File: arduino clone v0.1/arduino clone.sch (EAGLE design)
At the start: 24 parts, among them J202 FTDI Breakout Header, U101 ATMEGA328P_TQFP, U201 CH340G

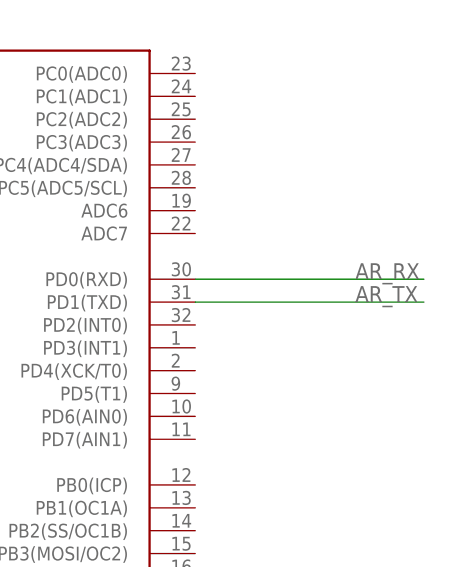
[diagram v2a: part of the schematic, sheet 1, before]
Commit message: connect MCU uart data lines to AR uart datalines
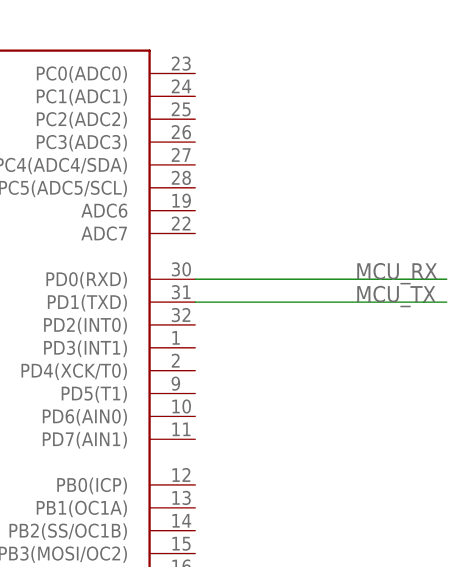
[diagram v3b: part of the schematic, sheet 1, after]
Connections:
- removed net AR_RX: R205.1, U101.PD0(RXD)
- removed net AR_TX: R206.1, U101.PD1(TXD)
- net MCU_RX: now also R205.1, U101.PD0(RXD)
- net MCU_TX: now also R206.1, U101.PD1(TXD)
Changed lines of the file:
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@@
 </segment>
 </net>
-<net name="AR_RX" class="0">
+<net name="MCU_RX" class="0">
 <segment>
 <pinref part="U101" gate="U$1" pin="PD0(RXD)"/>
 <wire x1="215.9" y1="139.7" x2="241.3" y2="139.7" width="0.1524" layer="91"/>
 <label x="233.68" y="139.7" size="1.778" layer="95"/>
-</segment>
-</net>
-<net name="AR_TX" class="0">
+<wire x1="241.3" y1="139.7" x2="243.84" y2="139.7" width="0.1524" layer="91"/>
+</segment>
+</net>
+<net name="MCU_TX" class="0">
 <segment>
 <pinref part="U101" gate="U$1" pin="PD1(TXD)"/>
 <wire x1="215.9" y1="137.16" x2="241.3" y2="137.16" width="0.1524" layer="91"/>
 <label x="233.68" y="137.16" size="1.778" layer="95"/>
+<wire x1="241.3" y1="137.16" x2="243.84" y2="137.16" width="0.1524" layer="91"/>
 </segment>
 </net>
@@
 </segment>
 </net>
-<net name="AR_RX" class="0">
-<segment>
-<pinref part="R205" gate="G$1" pin="1"/>
-<wire x1="312.42" y1="132.08" x2="320.04" y2="132.08" width="0.1524" layer="91"/>
-<wire x1="320.04" y1="132.08" x2="320.04" y2="129.54" width="0.1524" layer="91"/>
-<wire x1="320.04" y1="129.54" x2="350.52" y2="129.54" width="0.1524" layer="91"/>
-<label x="342.9" y="129.54" size="1.778" layer="95"/>
-</segment>
-</net>
-<net name="AR_TX" class="0">
-<segment>
-<pinref part="R206" gate="G$1" pin="1"/>
-<wire x1="312.42" y1="121.92" x2="320.04" y2="121.92" width="0.1524" layer="91"/>
-<wire x1="320.04" y1="121.92" x2="320.04" y2="124.46" width="0.1524" layer="91"/>
-<wire x1="320.04" y1="124.46" x2="350.52" y2="124.46" width="0.1524" layer="91"/>
-<label x="342.9" y="124.46" size="1.778" layer="95"/>
-</segment>
-</net>
 <net name="CH340G_DTR" class="0">
 <segment>
@@
 <label x="279.4" y="53.34" size="1.778" layer="95"/>
 </segment>
+<segment>
+<pinref part="R205" gate="G$1" pin="1"/>
+<wire x1="312.42" y1="132.08" x2="320.04" y2="132.08" width="0.1524" layer="91"/>
+<wire x1="320.04" y1="132.08" x2="320.04" y2="129.54" width="0.1524" layer="91"/>
+<wire x1="320.04" y1="129.54" x2="350.52" y2="129.54" width="0.1524" layer="91"/>
+<label x="342.9" y="129.54" size="1.778" layer="95"/>
+</segment>
 </net>
 <net name="FDTI_TX" class="0">
@@
 <label x="279.4" y="43.18" size="1.778" layer="95"/>
 </segment>
-</net>
+<segment>
+<pinref part="R206" gate="G$1" pin="1"/>
+<wire x1="312.42" y1="121.92" x2="320.04" y2="121.92" width="0.1524" layer="91"/>
+<wire x1="320.04" y1="121.92" x2="320.04" y2="124.46" width="0.1524" layer="91"/>
+<wire x1="320.04" y1="124.46" x2="350.52" y2="124.46" width="0.1524" layer="91"/>
+<label x="342.9" y="124.46" size="1.778" layer="95"/>
+</segment>
+</net>

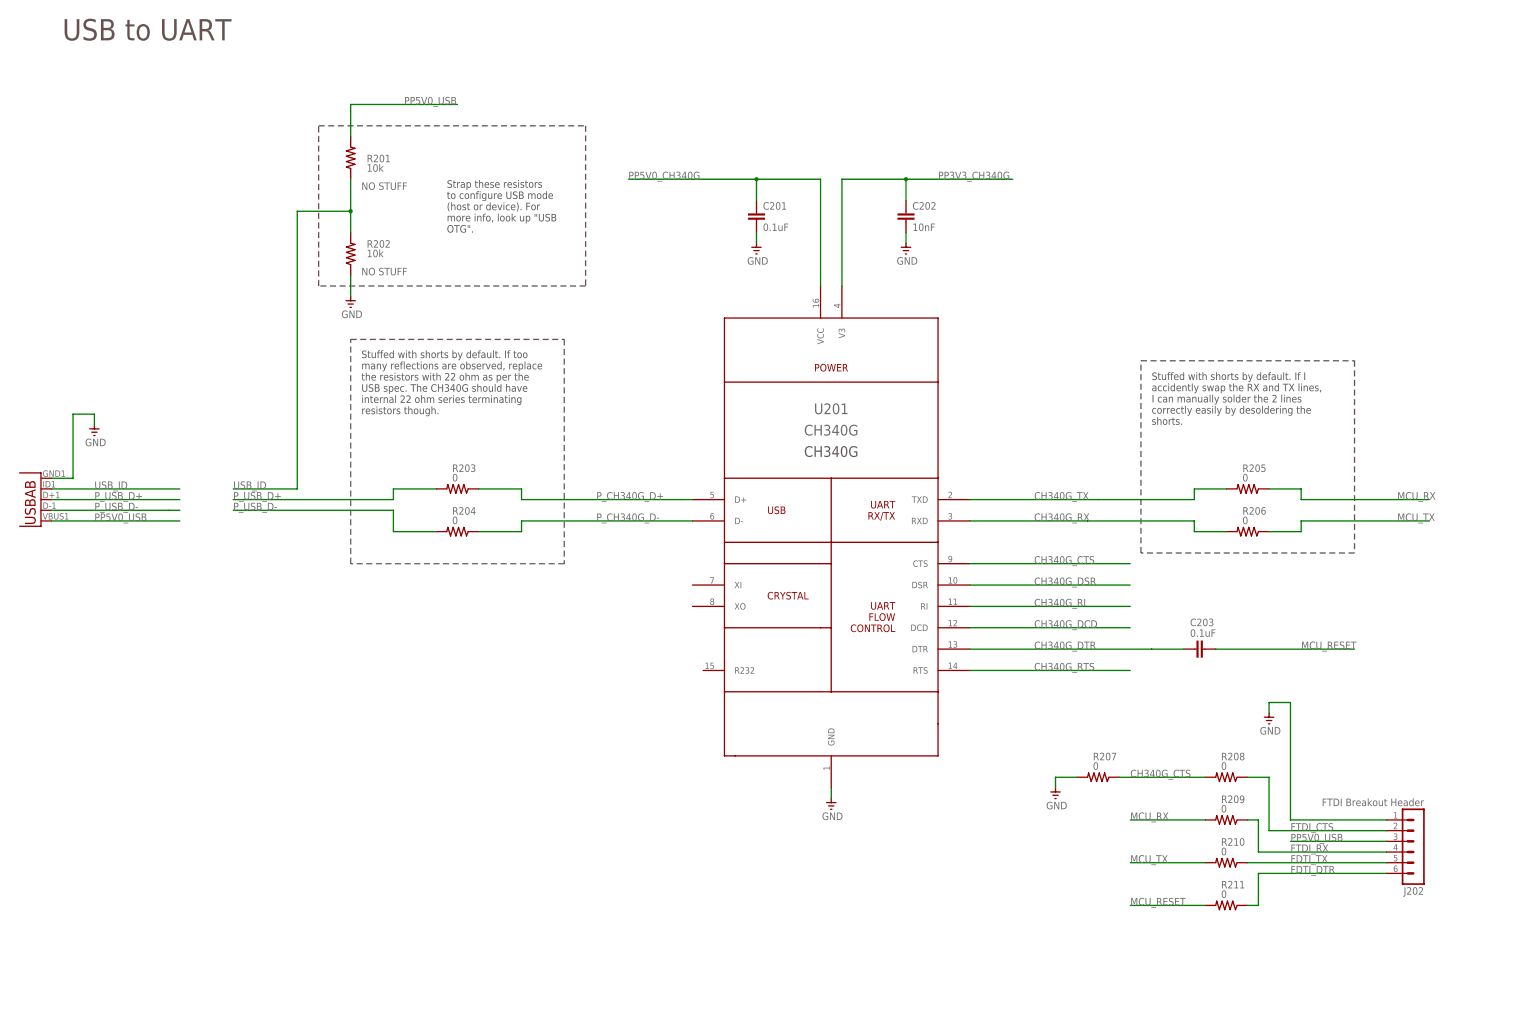
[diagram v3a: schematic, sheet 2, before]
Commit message: add notes for FTDI breakout headers
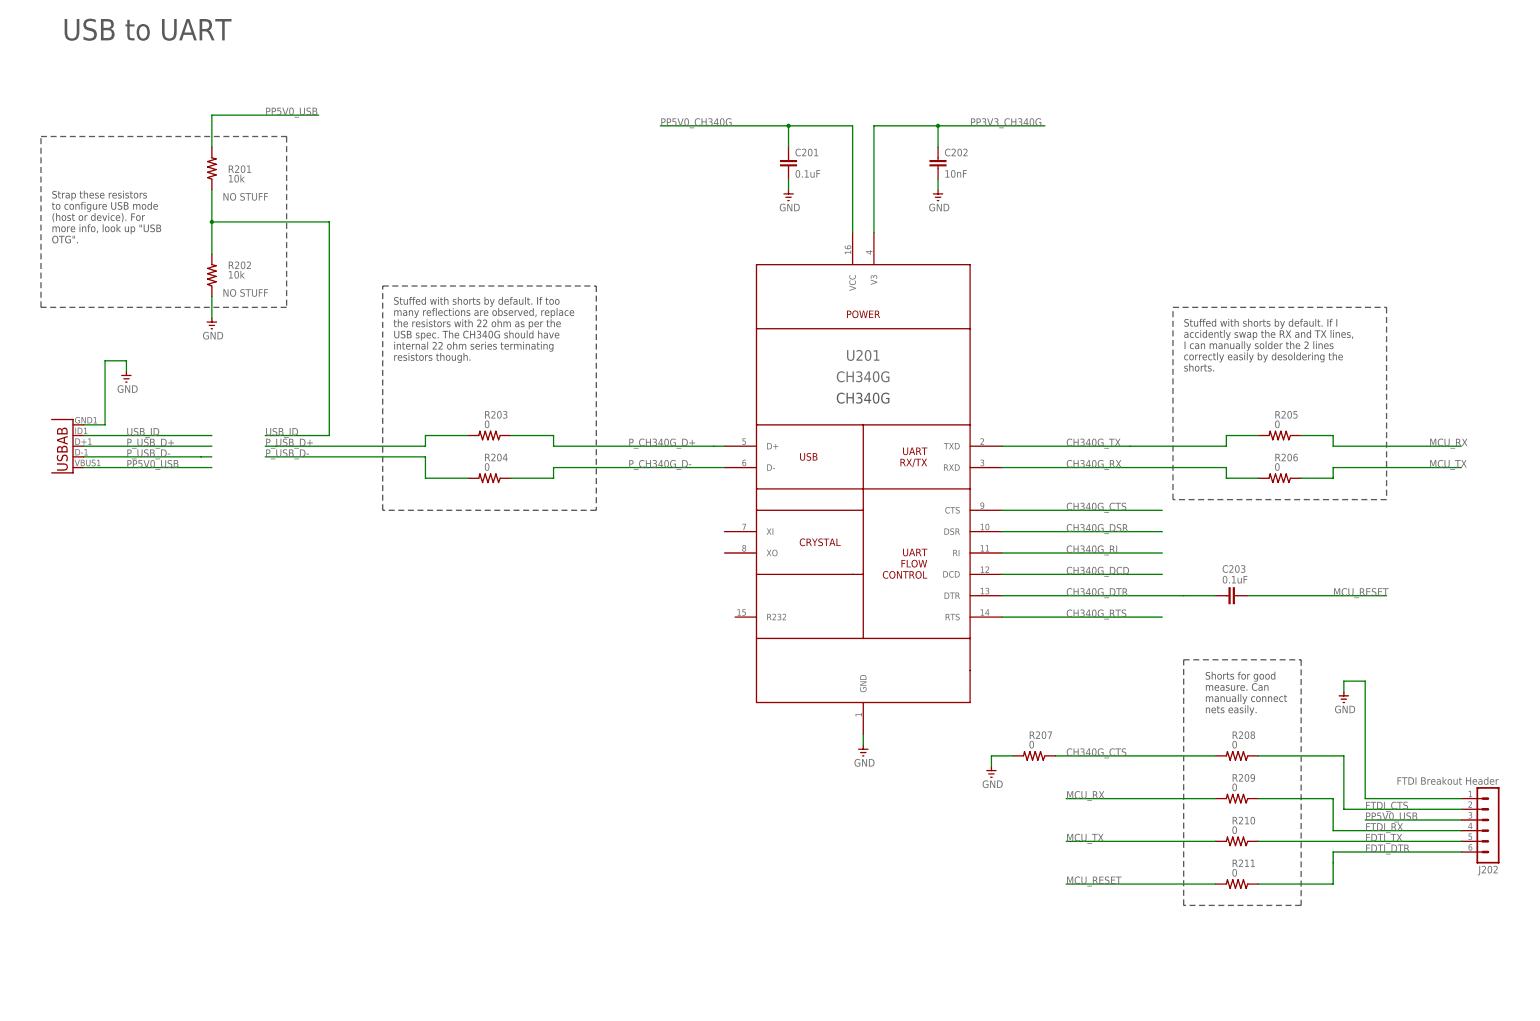
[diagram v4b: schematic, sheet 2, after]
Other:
- note added: "Shorts for good measure. Can manually connect nets easily."
- moved on the sheet: C201, C202, C203, J202, R201, R202, R203, R204, R205, R206, R207, R208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

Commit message: add note on CTS line
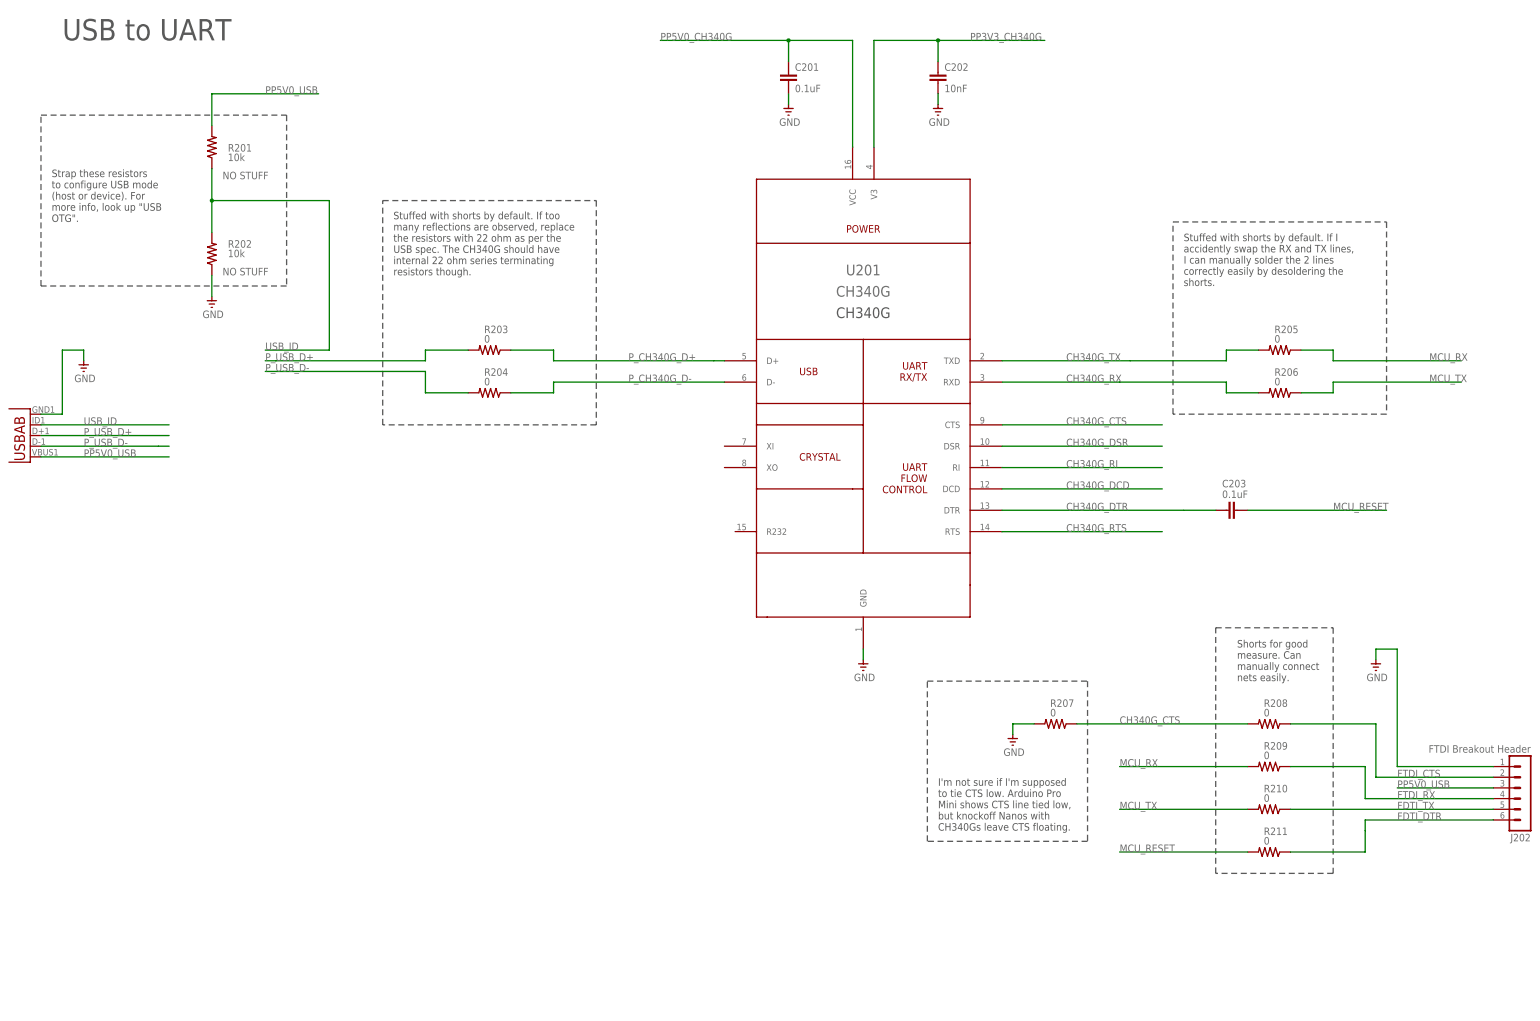
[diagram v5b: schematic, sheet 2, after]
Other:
- note added: "I'm not sure if I'm supposed to tie CTS low. Arduino Pro Mini shows CTS line tied low, but knockoff Nanos with CH340Gs leave CTS floating."
- moved on the sheet: C201, C202, C203, J202, R201, R202, R203, R204, R205, R206, R207, R208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

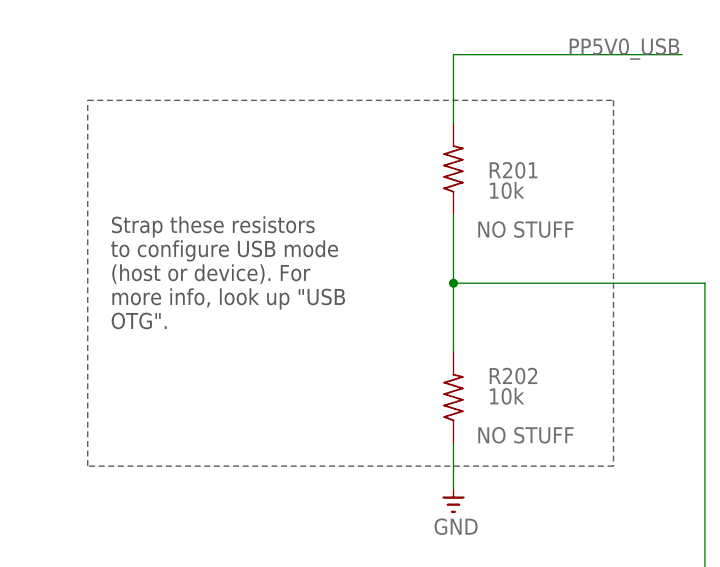
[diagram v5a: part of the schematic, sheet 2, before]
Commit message: update libs to fix R232 short pin
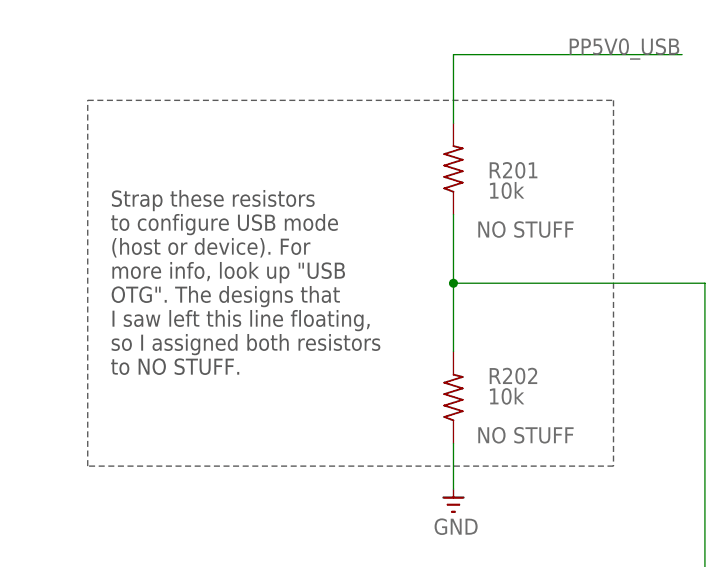
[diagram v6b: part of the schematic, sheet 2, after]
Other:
- note added: "Strap these resistors to configure USB mode (host or device). For more info, look up "USB OTG". The designs that I saw left this line floating, so I assigned both resistors to NO STUFF."
- note removed: "Strap these resistors to configure USB mode (host or device). For more info, look up "USB OTG"."
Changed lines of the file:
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@@
 <wire x1="78.74" y1="180.34" x2="20.32" y2="180.34" width="0.1524" layer="97" style="shortdash"/>
 <wire x1="20.32" y1="180.34" x2="20.32" y2="220.98" width="0.1524" layer="97" style="shortdash"/>
-<text x="22.86" y="195.58" size="1.778" layer="97">Strap these resistors
+<text x="22.86" y="190.5" size="1.778" layer="97">Strap these resistors
 to configure USB mode
 (host or device). For
 more info, look up "USB
-OTG".</text>
+OTG". The designs that
+I saw left this line floating,
+so I assigned both resistors
+to NO STUFF.</text>
 <wire x1="101.6" y1="200.66" x2="152.4" y2="200.66" width="0.1524" layer="97" style="shortdash"/>
 <wire x1="152.4" y1="200.66" x2="152.4" y2="147.32" width="0.1524" layer="97" style="shortdash"/>
